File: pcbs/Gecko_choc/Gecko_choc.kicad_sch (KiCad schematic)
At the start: 0 parts

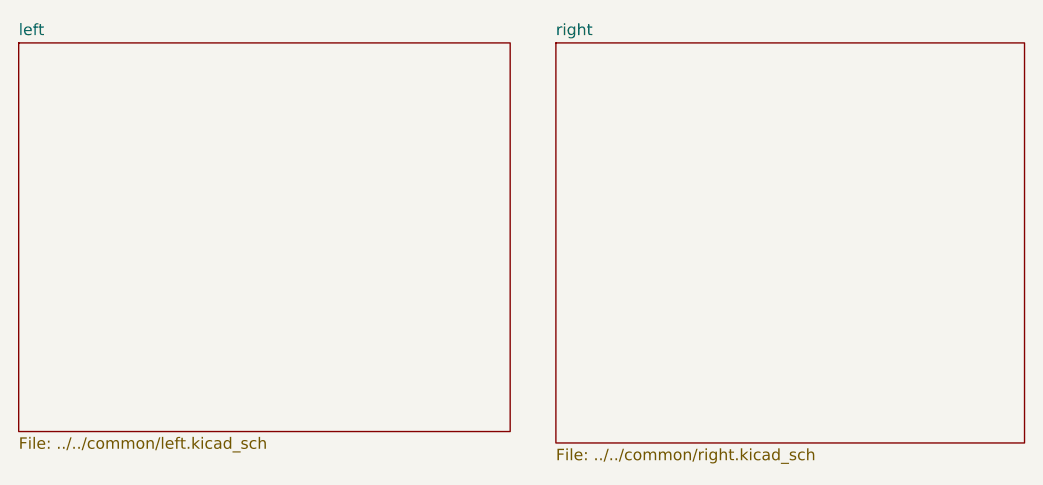
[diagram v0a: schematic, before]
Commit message: moved subsheets across
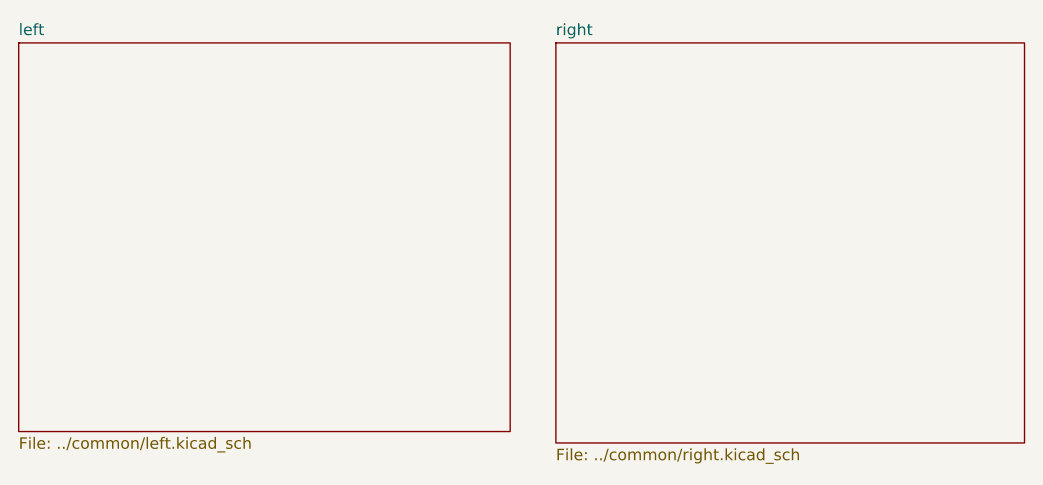
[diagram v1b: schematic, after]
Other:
- sheet left: file ../../common/left.kicad_sch -> ../common/left.kicad_sch
- sheet right: file ../../common/right.kicad_sch -> ../common/right.kicad_sch
- company: foostan -> Dane Evans
- title: Corne -> Gecko kbd
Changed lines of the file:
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@@
 	(paper "A5")
 	(title_block
-		(title "Corne")
+		(title "Gecko kbd")
 		(date "2024-05-07")
-		(rev "4.1.0")
-		(company "foostan")
+		(rev "1.0.0")
+		(company "Dane Evans")
+		(comment 1 "original: foostan's crkbd 4.1")
 	)
 	(sheet
@@
 			)
 		)
-		(property "Sheetfile" "../../common/left.kicad_sch"
+		(property "Sheetfile" "../common/left.kicad_sch"
 			(at 26.67 81.8646 0)
 			(effects
@@
 		)
 		(instances
-			(project "corne-chocolate"
+			(project "Gecko_choc"
 				(path "/4cc5d416-57f5-4147-8183-e03ae6b1198a"
 					(page "2")
@@
 			)
 		)
-		(property "Sheetfile" "../../common/right.kicad_sch"
+		(property "Sheetfile" "../common/right.kicad_sch"
 			(at 86.36 83.1346 0)
 			(effects
@@
 		)
 		(instances
-			(project "corne-chocolate"
+			(project "Gecko_choc"
 				(path "/4cc5d416-57f5-4147-8183-e03ae6b1198a"
 					(page "3")
